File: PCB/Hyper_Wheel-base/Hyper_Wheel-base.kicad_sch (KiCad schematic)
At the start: 10 parts, among them J1 I2C OLED CONN, SW1 SW_SPST, SW2 SW_SPST, SW3 SW_SPST, SW4 SW_SPST, SW5 SW_SPST, SW6 SW_SPST, U2 NRF52840-QFAA-R7, U3 AS5600L-ASOM, U8 DRV5032FCDBZR

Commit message: Base Push
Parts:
- removed J1: I2C OLED CONN, symbol Connector:Conn_01x04_Socket
- removed SW1, SW2, SW3, SW4, SW5, SW6: SW_SPST, symbol Switch:SW_SPST
- removed U2: NRF52840-QFAA-R7, QFN48_NRF52840-QFAA-R7_NOR, symbol NRF52840_QFAA_R7:NRF52840-QFAA-R7
- removed U3: AS5600L-ASOM, AS5600L-ASOM_AMS, symbol AS5600L_ASOM:AS5600L-ASOM
- removed U8: DRV5032FCDBZR, DBZ0003A-IPC_A, symbol DRV5032FCDBZR:DRV5032FCDBZR
- added AE1: Antenna, Hyper_Wheel:28mm Linear ANT, symbol Device:Antenna
- added D1: D_TVS, symbol Device:D_TVS
- added J3: USB4215-03-A, Hyper_Wheel:USBC-CONN_8p94X6p5X3p16_12L_GCC, symbol Hyper_Wheel:USB4215-03-A
- added RCC1, RCC2: 5.1k, Resistor_SMD:R_0402_1005Metric, symbol Device:R
- added RUSB1, RUSB2: 22, Resistor_SMD:R_0402_1005Metric, symbol Device:R
- added R_I2c_1, R_I2c_2, R_I2c_3, R_I2c_4: 4.7k, Resistor_SMD:R_0402_1005Metric, symbol Device:R
- added SW1, SW2: SW_Push, Button_Switch_SMD:SW_SPST_PTS647_Sx38, symbol Switch:SW_Push
- added U11: TPD2EUSB30ADRTR, Package_TO_SOT_SMD:SOT-323_SC-70, symbol Hyper_Wheel:TPD2EUSB30ADRTR
- added U17: 2450AT07A0100T, Hyper_Wheel:2450AT07A0100T_JOT, symbol Hyper_Wheel:2450AT07A0100T
- added U2: NRF52840-QIAA-R7, Hyper_Wheel:NORDIC_NRF52840-QIAA-R7, symbol Hyper_Wheel:NRF52840-QIAA-R7
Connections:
- net 3.3V_Regulated: now also R_I2c_1.1, R_I2c_2.1, R_I2c_3.2, R_I2c_4.2
- net GND: now also D1.2 (A2), J3.13 (GND), J3.14 (GND), J3.15 (GND), J3.16 (GND), J3.A1/B12 (GND), J3.B1/A12 (GND), RCC1.2, RCC2.2, SW1.1, SW2.2, U11.3 (GND), U17.2 (GND), U17.3 (GND)
- new net: SW1.2, U2.AC13 (P0.18/~{RESET})
- new net: RUSB2.1, U2.AD4 (D-)
- new net: RUSB1.1, U2.AD6 (D+)
- new net: J3.A5 (CC1), RCC1.1
- new net: J3.B5 (CC2), RCC2.1
- new net Cell_monitor: U2.J1 (P0.04/AIN2)
- new net D+: J3.A6 (DP1), J3.B6 (DP2), RUSB1.2, U11.1 (D+)
- new net D-: J3.A7 (DN1), J3.B7 (DN2), RUSB2.2, U11.2 (D-)
- new net Hall_1: U2.U1 (P0.12)
- new net I2C_1_SCL: R_I2c_2.2, U2.K2 (P0.05/AIN3)
- new net I2C_1_SDA: R_I2c_1.2, U2.M2 (P0.07)
- new net I2C_2_SCL: R_I2c_4.1, U2.AD20 (P0.24)
- new net I2C_2_SDA: R_I2c_3.1, U2.AD18 (P0.22)
- new net Key1: U2.Y23 (P1.01)
- new net Key2: U2.V23 (P1.03)
- new net Key3: U2.T23 (P1.05)
- new net Key4: U2.P23 (P1.07)
- new net Key5: U2.B13 (P0.03/AIN1)
- new net Key6: U2.B15 (P1.14)
- new net Key7: U2.B17 (P1.12)
- new net Key8: U2.B19 (P1.11)
- new net Load1 CTRL: U2.U24 (P1.04)
- new net Load2 CTRL: U2.R24 (P1.06)
- new net Load3 CTRL: U2.AD16 (P0.20)
- new net MCU_RF/PWR (page 3)/To_Antenna: U17.1 (FEED), U17.4 (FEED)
- new net USB Vbus: D1.1 (A1), J3.A4/B9 (VBUS), J3.B4/A9 (VBUS)
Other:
- added sheet MCU_RF/PWR (page 3) (MCU_Core.kicad_sch)
- added sheet Peripherals (Peripherals.kicad_sch)
- sheet Power Handling ports: added Cell-Mon, Charger+, Load1_Ctrl, Load1_Vout, Load2_Ctrl, Load2_Vout, Load3_Ctrl, Load3_Vout; removed none

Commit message: Missing TVS Diode places
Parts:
- D1: footprint (none) -> Diode_SMD:D_0603_1608Metric
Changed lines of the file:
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@@
 			)
 		)
-		(property "Footprint" ""
+		(property "Footprint" "Diode_SMD:D_0603_1608Metric"
 			(at 243.84 59.69 0)
 			(hide yes)

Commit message: Updated work on antenna, And adjusted log structure
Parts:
- U17: footprint Hyper_Wheel:2450AT07A0100T_JOT -> Hyper_Wheel:2450AT07A0100T_JOT+Keepout
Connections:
- net MCU_RF/PWR (page 3)/To_Antenna renamed AntFeed
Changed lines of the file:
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@@
 	(wire
 		(pts
-			(xy 97.79 157.48) (xy 97.79 147.32)
-		)
-		(stroke
-			(width 0)
-			(type default)
-		)
-	)
-	(wire
-		(pts
 			(xy 77.47 147.32) (xy 97.79 147.32)
 		)
@@
 	(wire
 		(pts
+			(xy 97.79 146.05) (xy 97.79 161.29)
+		)
+		(stroke
+			(width 0)
+			(type default)
+		)
+	)
+	(wire
+		(pts
 			(xy 243.84 63.5) (xy 264.16 63.5)
 		)
@@
 		)
 	)
+	(label "AntFeed"
+		(at 77.47 130.81 0)
+		(effects
+			(font
+				(size 1.27 1.27)
+			)
+			(justify left bottom)
+		)
+	)
 	(label "Load2 V"
 		(at 129.54 172.72 90)
@@
 	(symbol
 		(lib_id "power:GND")
-		(at 97.79 157.48 0)
+		(at 97.79 161.29 0)
 		(unit 1)
 		(body_style 1)
@@
 		(fields_autoplaced yes)
 		(property "Reference" "#PWR027"
-			(at 97.79 163.83 0)
+			(at 97.79 167.64 0)
 			(hide yes)
 			(show_name no)
@@
 		)
 		(property "Value" "GND"
-			(at 97.79 162.56 0)
+			(at 97.79 166.37 0)
 			(show_name no)
 			(do_not_autoplace no)
@@
 		)
 		(property "Footprint" ""
-			(at 97.79 157.48 0)
+			(at 97.79 161.29 0)
 			(hide yes)
 			(show_name no)
@@
 		)
 		(property "Datasheet" ""
-			(at 97.79 157.48 0)
+			(at 97.79 161.29 0)
 			(hide yes)
 			(show_name no)
@@
 		)
 		(property "Description" "Power symbol creates a global label with name \"GND\" , ground"
-			(at 97.79 157.48 0)
+			(at 97.79 161.29 0)
 			(hide yes)
 			(show_name no)
@@
 			)
 		)
-		(property "Footprint" "Hyper_Wheel:2450AT07A0100T_JOT"
+		(property "Footprint" "Hyper_Wheel:2450AT07A0100T_JOT+Keepout"
 			(at 77.47 144.78 0)
 			(hide yes)

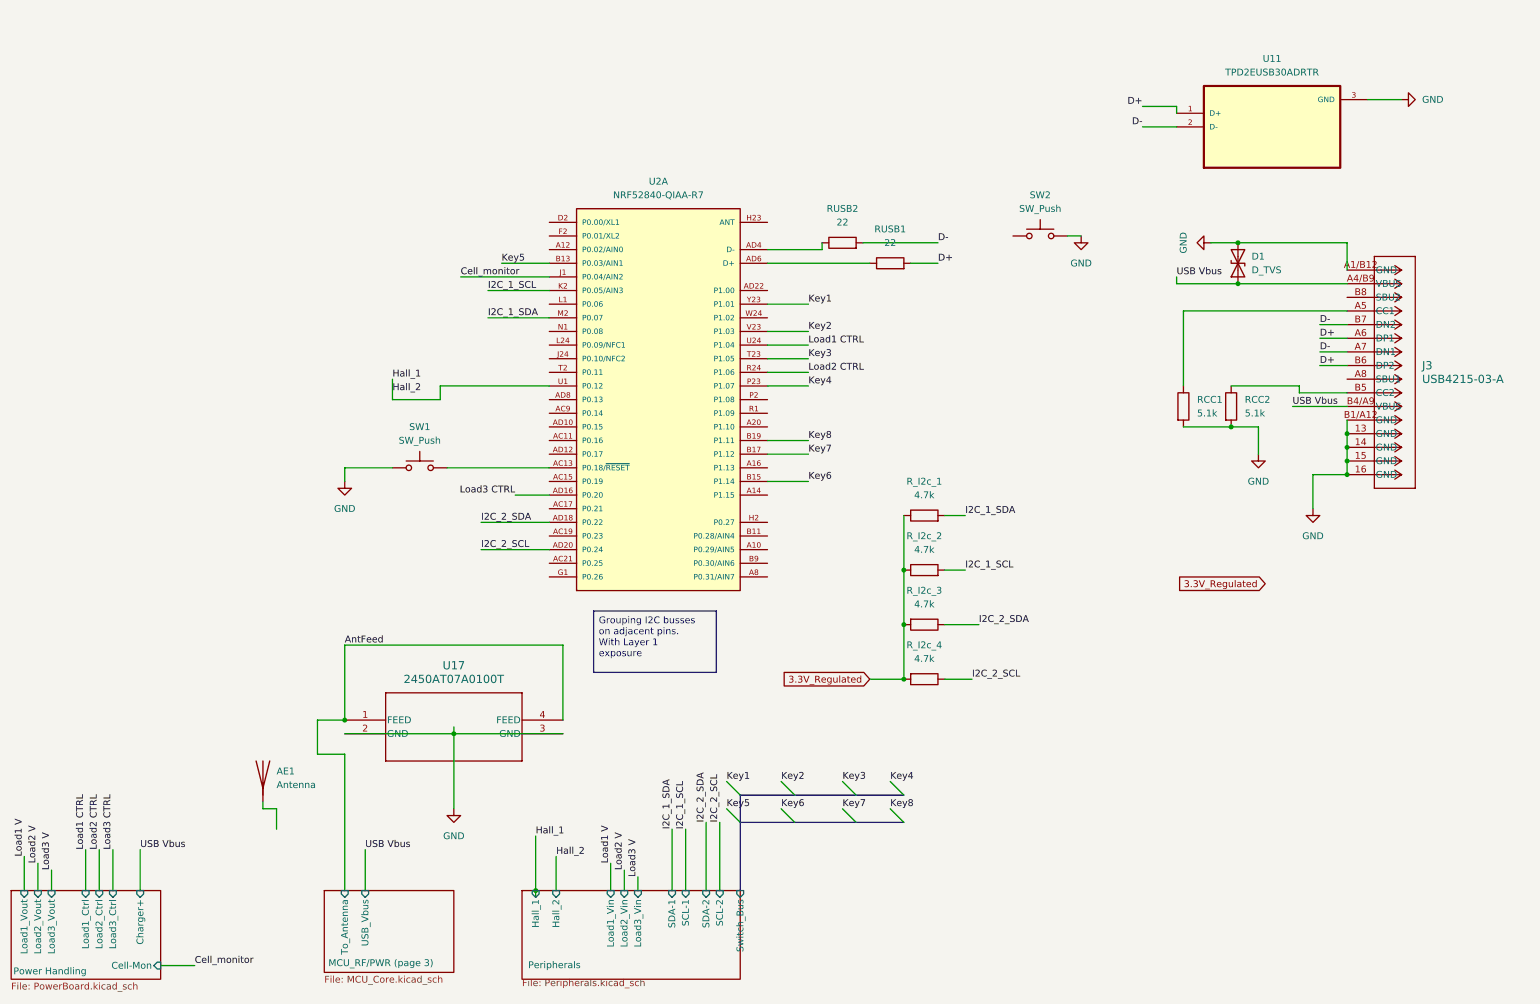
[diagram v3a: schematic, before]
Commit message: Main board nearing RevA completion
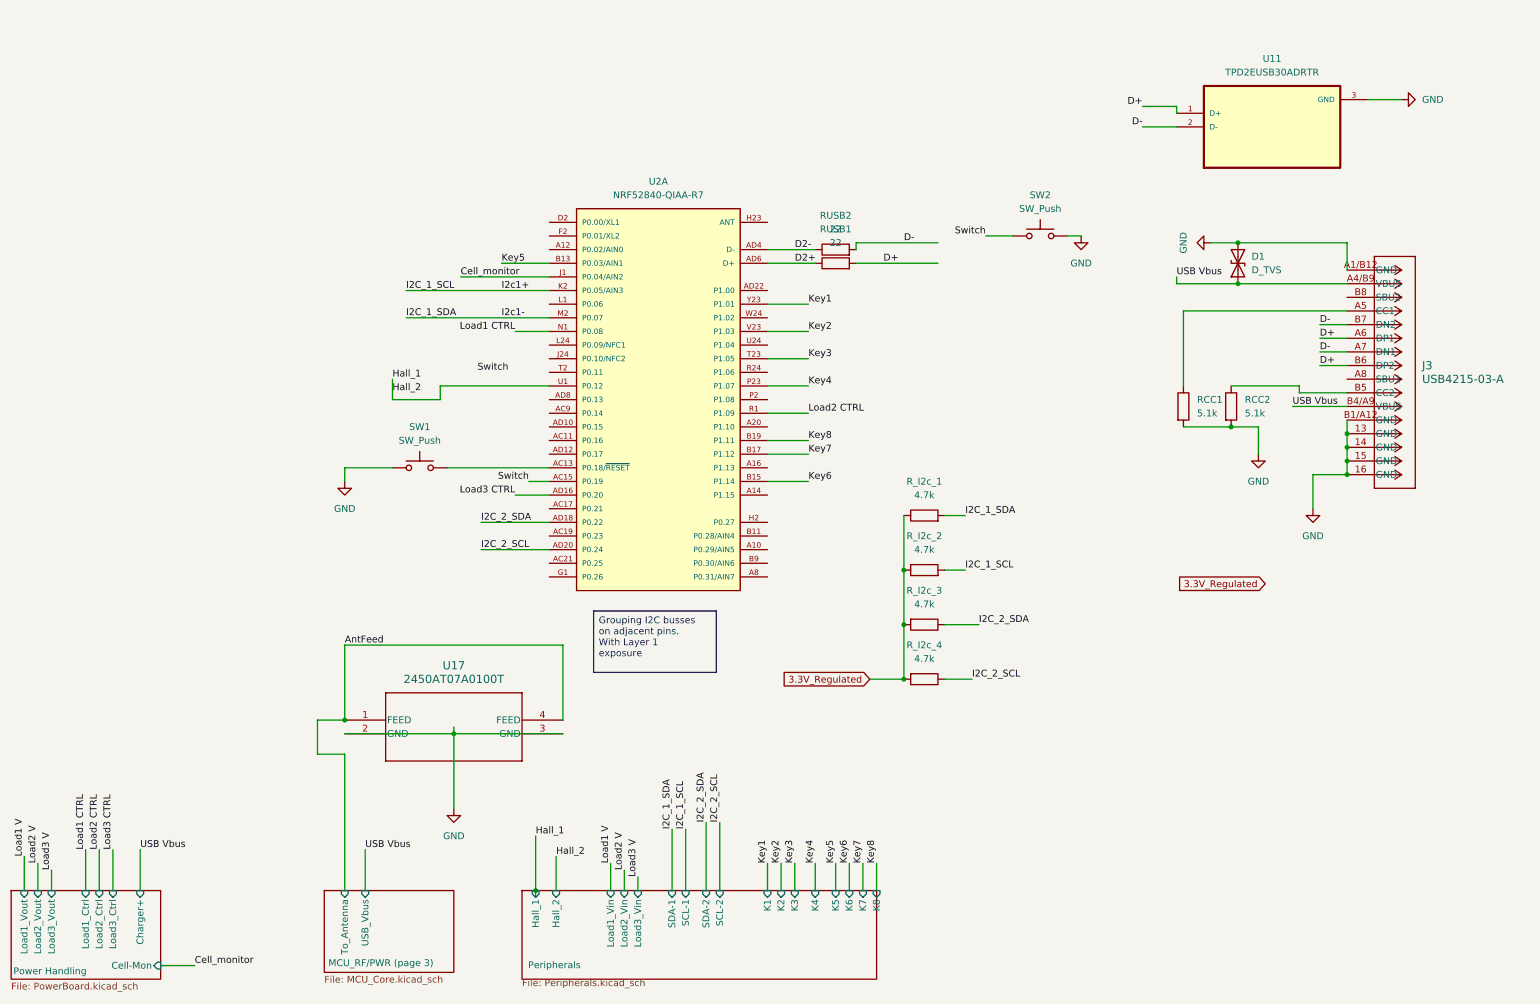
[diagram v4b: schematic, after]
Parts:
- removed AE1: Antenna, Hyper_Wheel:28mm Linear ANT, symbol Device:Antenna
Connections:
- net Load1 CTRL: now also U2.N1 (P0.08); no longer U2.U24 (P1.04)
- net Load2 CTRL: now also U2.R1 (P1.09); no longer U2.R24 (P1.06)
- net Switch: now reaches SW2.1
- net Switch: now also U2.AC15 (P0.19)
- net D2-: now reaches RUSB2.1, U2.AD4 (D-)
- net D2+: now reaches RUSB1.1, U2.AD6 (D+)
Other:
- sheet Peripherals ports: added K1, K2, K3, K4, K5, K6, K7, K8; removed Switch_Bus
- moved on the sheet: RUSB1, RUSB2

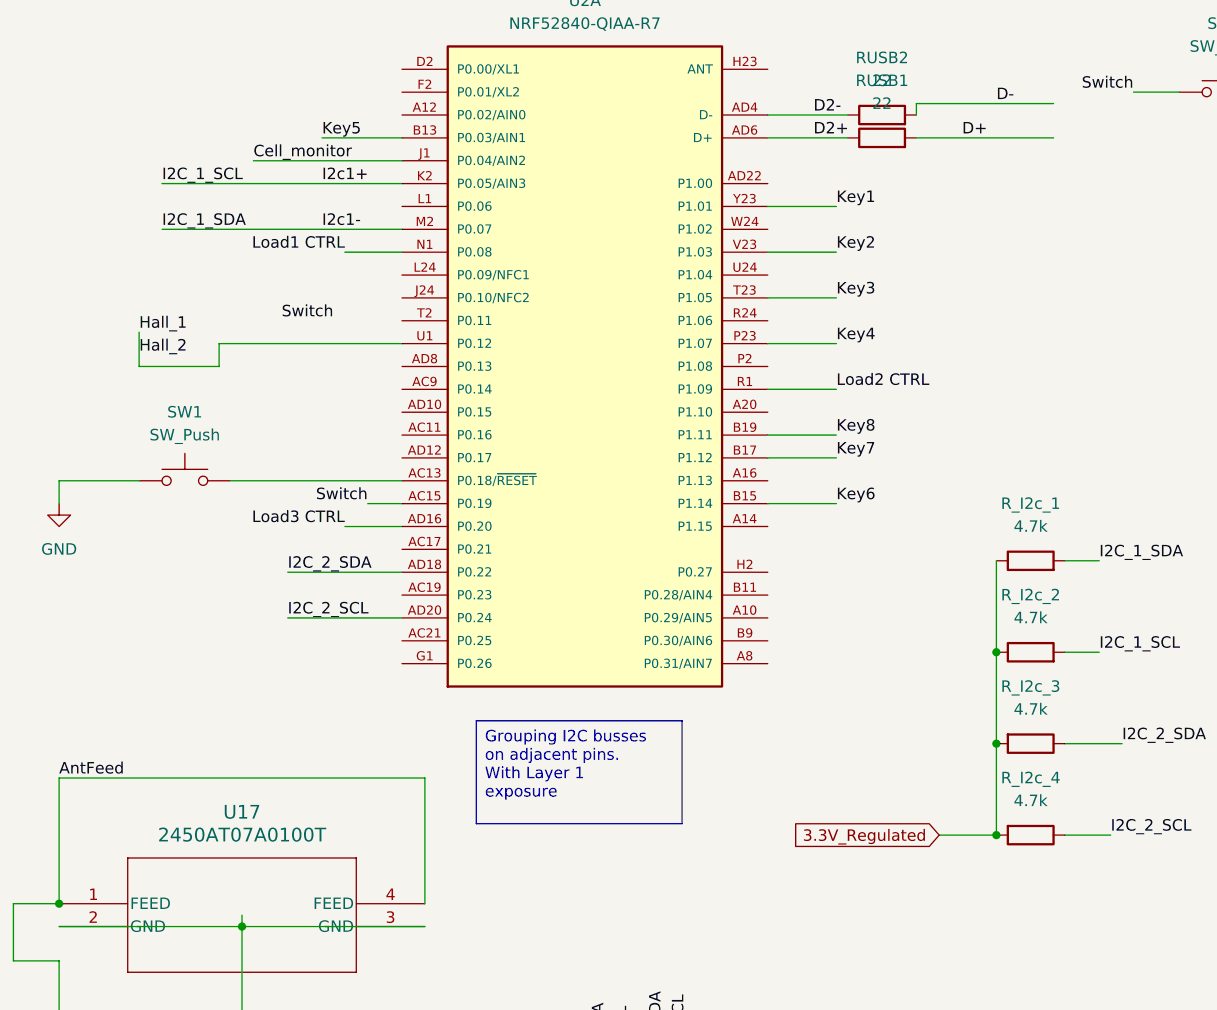
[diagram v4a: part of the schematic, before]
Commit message: power plane added,  passes Peer review
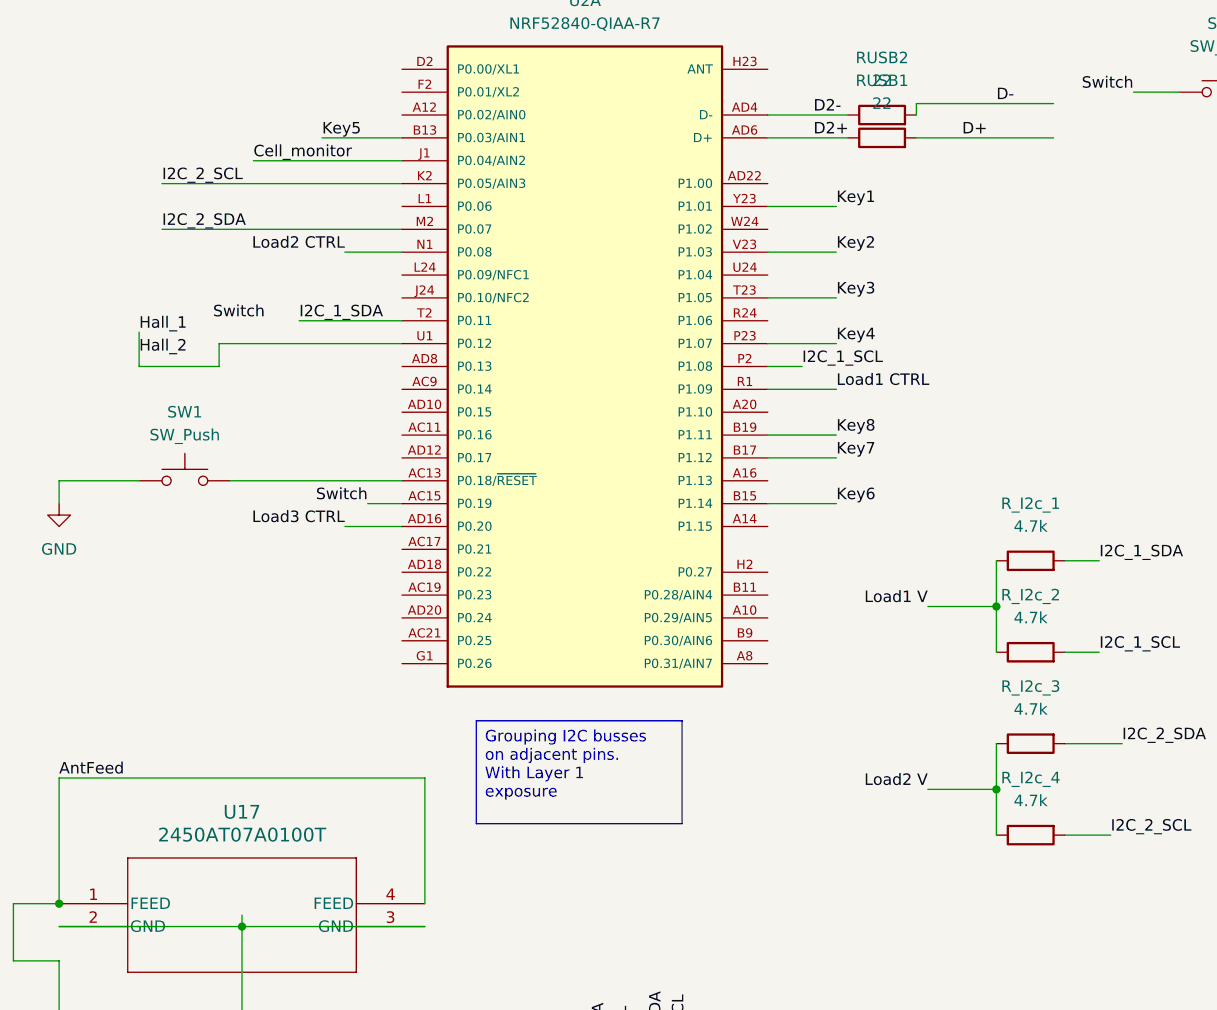
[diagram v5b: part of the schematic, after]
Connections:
- net 3.3V_Regulated: no longer R_I2c_1.1, R_I2c_2.1, R_I2c_3.2, R_I2c_4.2
- net I2C_1_SCL: now also U2.P2 (P1.08); no longer U2.K2 (P0.05/AIN3)
- net I2C_1_SDA: now also U2.T2 (P0.11); no longer U2.M2 (P0.07)
- net I2C_2_SCL: now also R_I2c_4.2, U2.K2 (P0.05/AIN3); no longer R_I2c_4.1, U2.AD20 (P0.24)
- net I2C_2_SDA: now also R_I2c_3.2, U2.M2 (P0.07); no longer R_I2c_3.1, U2.AD18 (P0.22)
- net Load1 CTRL: now also U2.R1 (P1.09); no longer U2.N1 (P0.08)
- net Load1 V: now also R_I2c_1.1, R_I2c_2.1
- net Load2 CTRL: now also U2.N1 (P0.08); no longer U2.R1 (P1.09)
- net Load2 V: now also R_I2c_3.1, R_I2c_4.1
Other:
- moved on the sheet: R_I2c_3, R_I2c_4
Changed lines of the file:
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@@
 	)
 	(junction
-		(at 181.61 116.84)
-		(diameter 0)
-		(color 0 0 0 0)
-	)
-	(junction
-		(at 181.61 127)
+		(at 181.61 111.76)
 		(diameter 0)
 		(color 0 0 0 0)
@@
 	)
 	(junction
-		(at 181.61 137.16)
+		(at 181.61 132.08)
 		(diameter 0)
 		(color 0 0 0 0)
@@
 	(wire
 		(pts
-			(xy 102.87 113.03) (xy 115.57 113.03)
-		)
-		(stroke
-			(width 0)
-			(type default)
-		)
-	)
-	(wire
-		(pts
 			(xy 109.22 72.39) (xy 115.57 72.39)
 		)
@@
 	(wire
 		(pts
-			(xy 102.87 107.95) (xy 115.57 107.95)
-		)
-		(stroke
-			(width 0)
-			(type default)
-		)
-	)
-	(wire
-		(pts
 			(xy 118.11 130.81) (xy 77.47 130.81)
 		)
@@
 	(wire
 		(pts
-			(xy 181.61 127) (xy 181.61 137.16)
+			(xy 181.61 127) (xy 181.61 132.08)
 		)
 		(stroke
@@
 	(wire
 		(pts
+			(xy 104.14 80.01) (xy 115.57 80.01)
+		)
+		(stroke
+			(width 0)
+			(type default)
+		)
+	)
+	(wire
+		(pts
 			(xy 132.08 173.99) (xy 132.08 176.53)
 		)
@@
 	(wire
 		(pts
-			(xy 175.26 137.16) (xy 181.61 137.16)
+			(xy 173.99 132.08) (xy 181.61 132.08)
 		)
 		(stroke
@@
 	(wire
 		(pts
+			(xy 173.99 111.76) (xy 181.61 111.76)
+		)
+		(stroke
+			(width 0)
+			(type default)
+		)
+	)
+	(wire
+		(pts
 			(xy 259.08 76.2) (xy 264.16 76.2)
 		)
@@
 	(wire
 		(pts
+			(xy 181.61 132.08) (xy 181.61 137.16)
+		)
+		(stroke
+			(width 0)
+			(type default)
+		)
+	)
+	(wire
+		(pts
 			(xy 196.85 54.61) (xy 201.93 54.61)
 		)
@@
 	(wire
 		(pts
+			(xy 181.61 111.76) (xy 181.61 116.84)
+		)
+		(stroke
+			(width 0)
+			(type default)
+		)
+	)
+	(wire
+		(pts
 			(xy 115.57 59.69) (xy 106.68 59.69)
 		)
@@
 	(wire
 		(pts
-			(xy 181.61 106.68) (xy 181.61 116.84)
+			(xy 156.21 85.09) (xy 160.02 85.09)
 		)
 		(stroke
@@
 	(wire
 		(pts
-			(xy 181.61 116.84) (xy 181.61 127)
+			(xy 181.61 106.68) (xy 181.61 111.76)
 		)
 		(stroke
@@
 	)
 	(label "I2C_2_SDA"
-		(at 102.87 107.95 0)
+		(at 88.9 69.85 0)
 		(effects
 			(font
@@
 	)
 	(label "I2C_1_SCL"
-		(at 88.9 64.77 0)
+		(at 160.02 85.09 0)
 		(effects
 			(font
@@
 		)
 	)
-	(label "I2c1+"
-		(at 106.68 64.77 0)
-		(effects
-			(font
-				(size 1.27 1.27)
-			)
-			(justify left bottom)
-		)
-	)
 	(label "AntFeed"
 		(at 77.47 130.81 0)
@@
 	)
 	(label "Switch"
-		(at 107.95 80.01 180)
+		(at 100.33 80.01 180)
 		(effects
 			(font
@@
 	)
 	(label "I2C_2_SCL"
-		(at 102.87 113.03 0)
+		(at 88.9 64.77 0)
 		(effects
 			(font
@@
 		)
 	)
-	(label "I2c1-"
-		(at 106.68 69.85 0)
-		(effects
-			(font
-				(size 1.27 1.27)
-			)
-			(justify left bottom)
-		)
-	)
 	(label "USB Vbus"
 		(at 232.41 62.23 0)
@@
 	)
 	(label "I2C_1_SDA"
-		(at 88.9 69.85 0)
+		(at 104.14 80.01 0)
 		(effects
 			(font
@@
 	)
 	(label "Load2 CTRL"
-		(at 163.83 87.63 0)
+		(at 109.22 72.39 180)
 		(effects
 			(font
 				(size 1.27 1.27)
 			)
-			(justify left bottom)
+			(justify right bottom)
 		)
 	)
@@
 	)
 	(label "Load1 CTRL"
-		(at 109.22 72.39 180)
+		(at 163.83 87.63 0)
+		(effects
+			(font
+				(size 1.27 1.27)
+			)
+			(justify left bottom)
+		)
+	)
+	(label "Load1 V"
+		(at 173.99 111.76 180)
 		(effects
 			(font
@@
 		)
 	)
-	(global_label "3.3V_Regulated"
-		(shape input)
-		(at 248.92 119.38 180)
-		(fields_autoplaced yes)
+	(label "Load2 V"
+		(at 173.99 132.08 180)
 		(effects
 			(font
 				(size 1.27 1.27)
 			)
-			(justify right)
-		)
-		(property "Intersheetrefs" "${INTERSHEET_REFS}"
-			(at 231.4207 119.38 0)
-			(hide yes)
-			(show_name no)
-			(do_not_autoplace no)
-			(effects
-				(font
-					(size 1.27 1.27)
-				)
-				(justify right)
-			)
+			(justify right bottom)
 		)
 	)
 	(global_label "3.3V_Regulated"
 		(shape input)
-		(at 175.26 137.16 180)
+		(at 248.92 119.38 180)
 		(fields_autoplaced yes)
 		(effects
@@
 		)
 		(property "Intersheetrefs" "${INTERSHEET_REFS}"
-			(at 157.7607 137.16 0)
+			(at 231.4207 119.38 0)
 			(hide yes)
 			(show_name no)
@@
 	(symbol
 		(lib_id "Device:R")
-		(at 185.42 127 270)
+		(at 185.42 127 90)
+		(mirror x)
 		(unit 1)
 		(body_style 1)
@@
 	(symbol
 		(lib_id "Device:R")
-		(at 185.42 137.16 270)
+		(at 185.42 137.16 90)
+		(mirror x)
 		(unit 1)
 		(body_style 1)

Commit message: Added test pads,
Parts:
- added P1: TestPad, TestPoint:TestPoint_Pad_D1.5mm, symbol Connector:Conn_01x01_Pin
- added P10, P11, P12, P15, P16, P2, P23, P24, P3, P4, P5, P6, P7, P8, P9: TestPad, TestPoint:TestPoint_Pad_D2.0mm, symbol Connector:Conn_01x01_Pin
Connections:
- net 3.3V_Regulated: now also P11.1 (Pin_1)
- net Cell_monitor: now also P9.1 (Pin_1)
- net GND: now also P15.1 (Pin_1), P16.1 (Pin_1)
- net Hall_1: now also P10.1 (Pin_1)
- net I2C_1_SCL: now also P2.1 (Pin_1)
- net I2C_1_SDA: now also P1.1 (Pin_1)
- net I2C_2_SCL: now also P3.1 (Pin_1)
- net I2C_2_SDA: now also P4.1 (Pin_1)
- net Load1 CTRL: now also P6.1 (Pin_1)
- net Load1 V: now also P5.1 (Pin_1)
- net Load2 CTRL: now also P8.1 (Pin_1)
- net Load2 V: now also P7.1 (Pin_1)
- net USB Vbus: now also P12.1 (Pin_1)
- net Spare1: now reaches U2.AC17 (P0.21)
- net Spare1: now also P23.1 (Pin_1)
- net Spare2: now reaches U2.AC19 (P0.23)
- net Spare2: now also P24.1 (Pin_1)
